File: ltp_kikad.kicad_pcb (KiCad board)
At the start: 2 copper layers, 65 x 56.5 mm, 21 parts, among them IC1 SamacSys_Parts_HT16K33-28SOP, IC2 SamacSys_Parts_HT16K33-28SOP, J2 RPi_GPIO

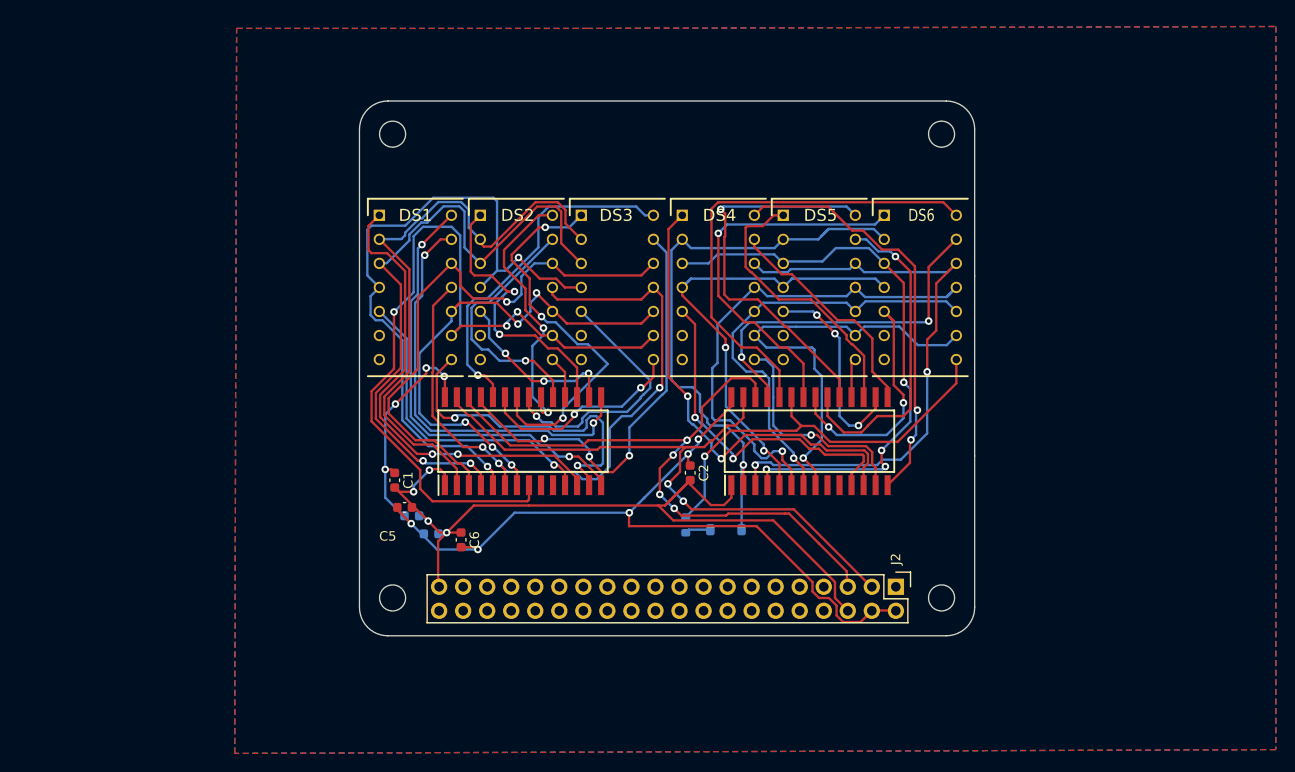
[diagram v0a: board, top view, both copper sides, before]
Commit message: Add 3d  device render
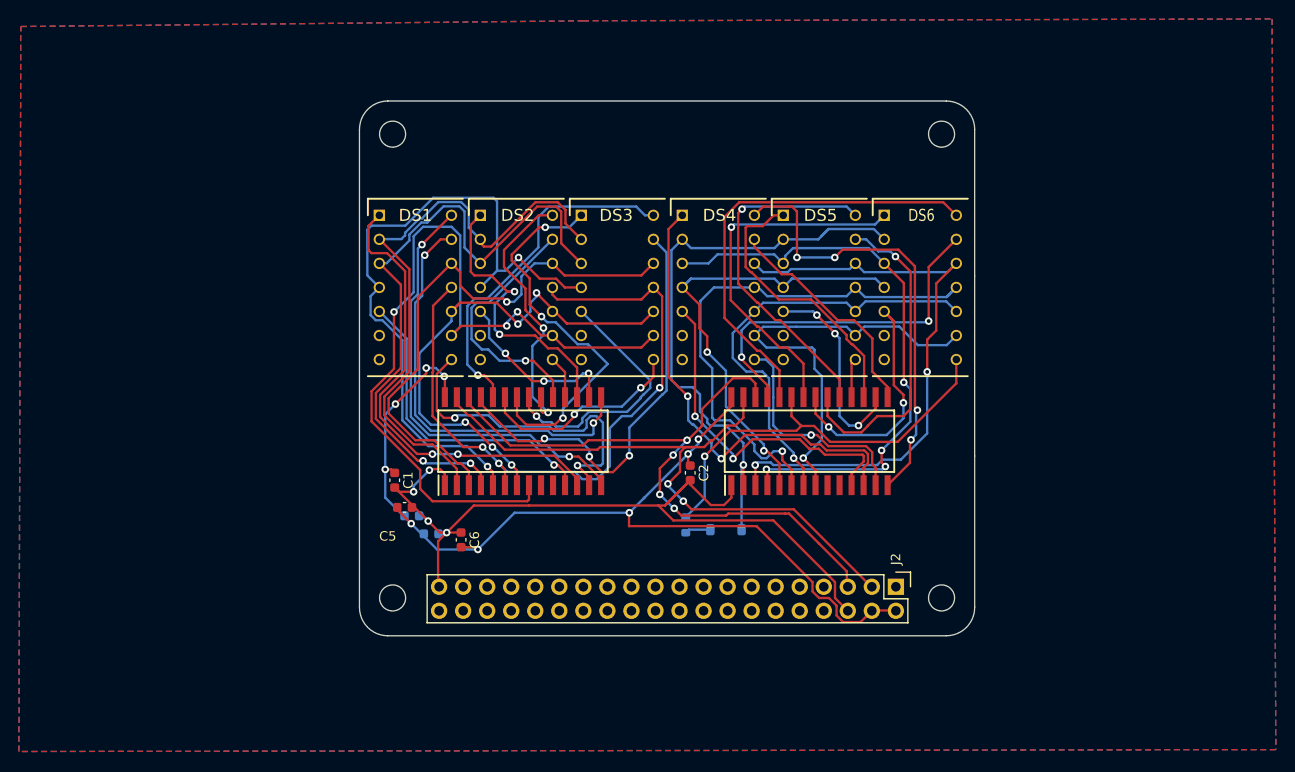
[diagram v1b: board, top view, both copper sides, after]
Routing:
- net 2_an6: track 42.2 -> 37.3 mm
- net 2_ca4: track 53.5 -> 57.0 mm
- net 2_an11: track 44.5 -> 48.0 mm, vias 2 -> 4
- net 2_an1: track 50.6 -> 47.3 mm
- net 2_an3: track 40.4 -> 38.4 mm

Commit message: Minimize vias transitions, optimize traces
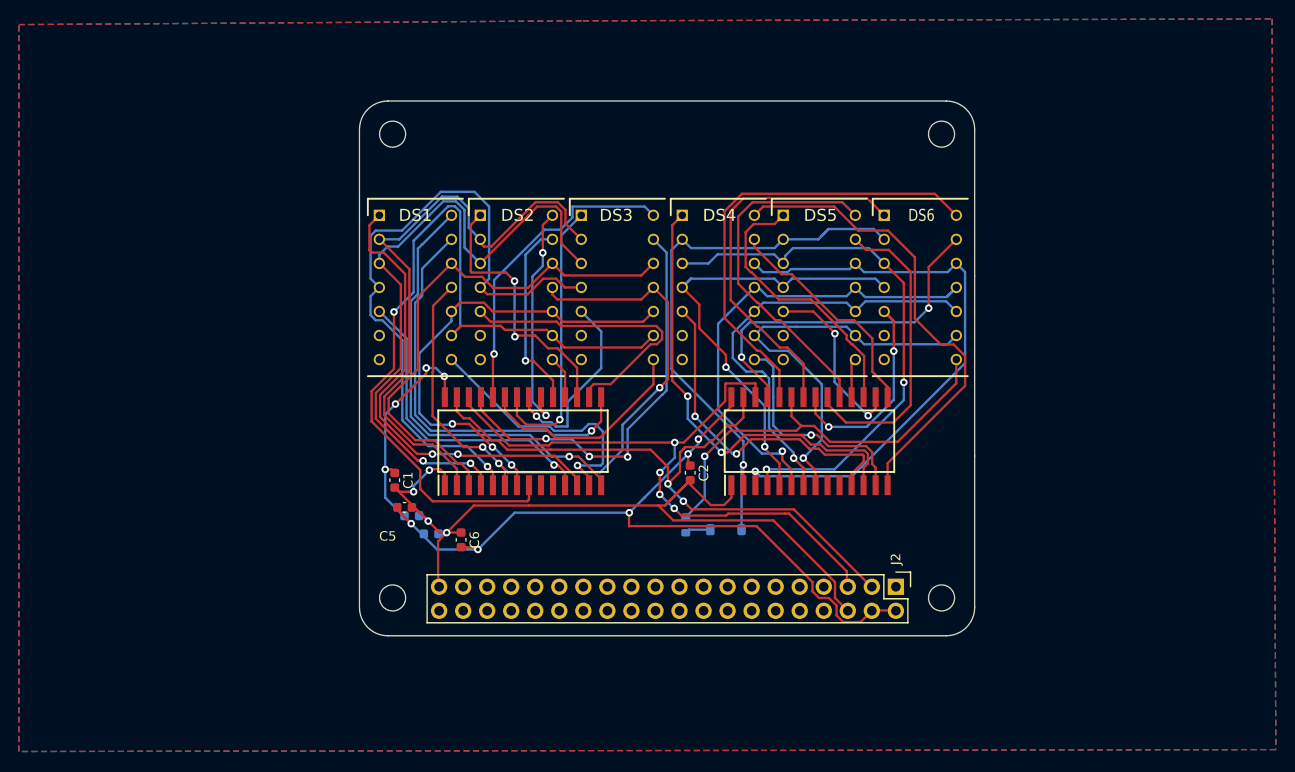
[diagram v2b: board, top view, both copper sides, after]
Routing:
- net an9: track 18.5 -> 31.7 mm, vias 3 -> 0
- net an3: track 41.2 -> 29.6 mm, vias 3 -> 1
- net an12: track 35.8 -> 28.5 mm, vias 2 -> 1
- net an4: track 27.9 -> 20.6 mm
- net an6: track 27.0 -> 20.2 mm
- net 2_ca4: track 57.0 -> 51.3 mm
- net an5: track 29.0 -> 24.8 mm
- net ca5: track 54.9 -> 50.9 mm, vias 5 -> 3
- net an1: track 37.4 -> 33.5 mm
- net 2_ca2: track 62.0 -> 58.1 mm, vias 4 -> 2
- net 2_an4: track 26.1 -> 22.8 mm
- net ca1: track 58.8 -> 55.6 mm, vias 1 -> 0
- net 2_an9: track 21.5 -> 18.9 mm, vias 3 -> 2
- net 2_an3: track 38.4 -> 41.0 mm, vias 1 -> 0
- net 2_ca6: track 46.7 -> 44.1 mm
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
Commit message: Minor improvements
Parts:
- moved J2 0.09 mm to (151.5, 105.6)
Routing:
- net SDA: track 68.5 -> 67.4 mm
- net +5V: track 108.7 -> 109.5 mm

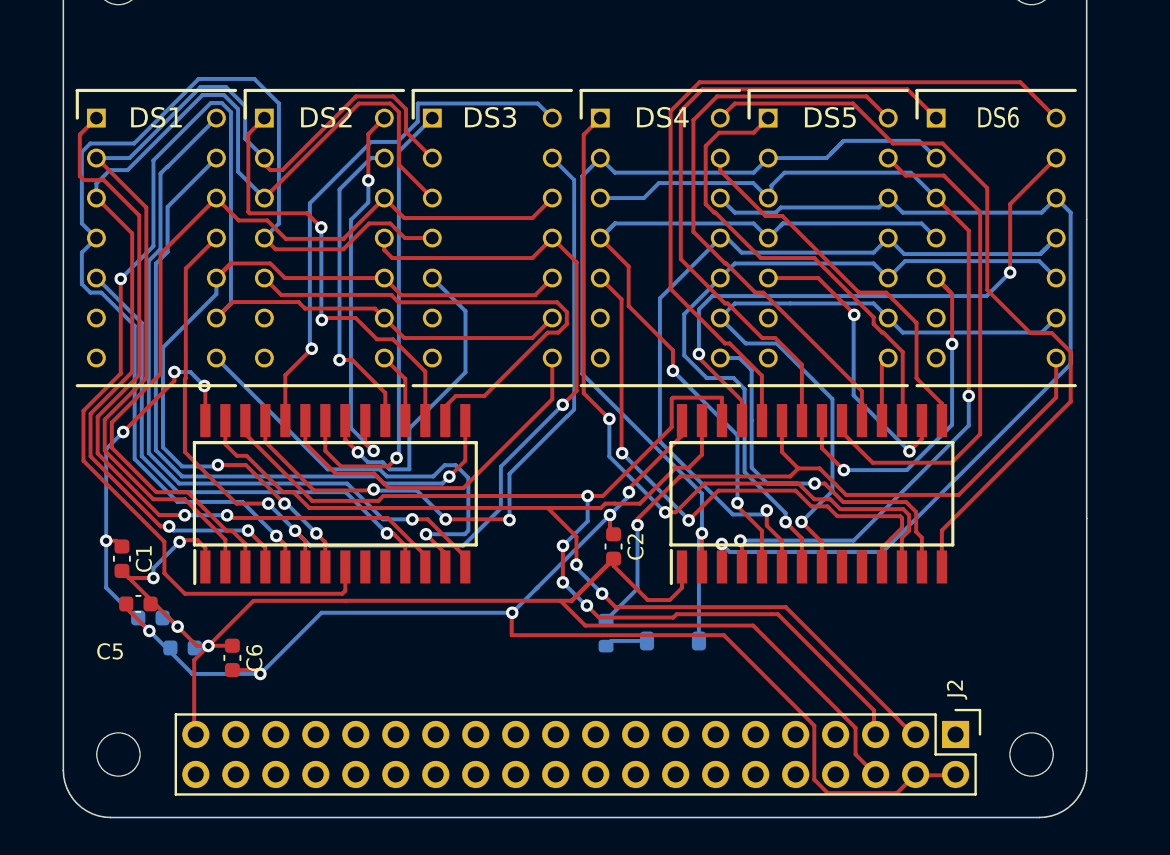
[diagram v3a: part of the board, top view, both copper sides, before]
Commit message: Add bypas cap
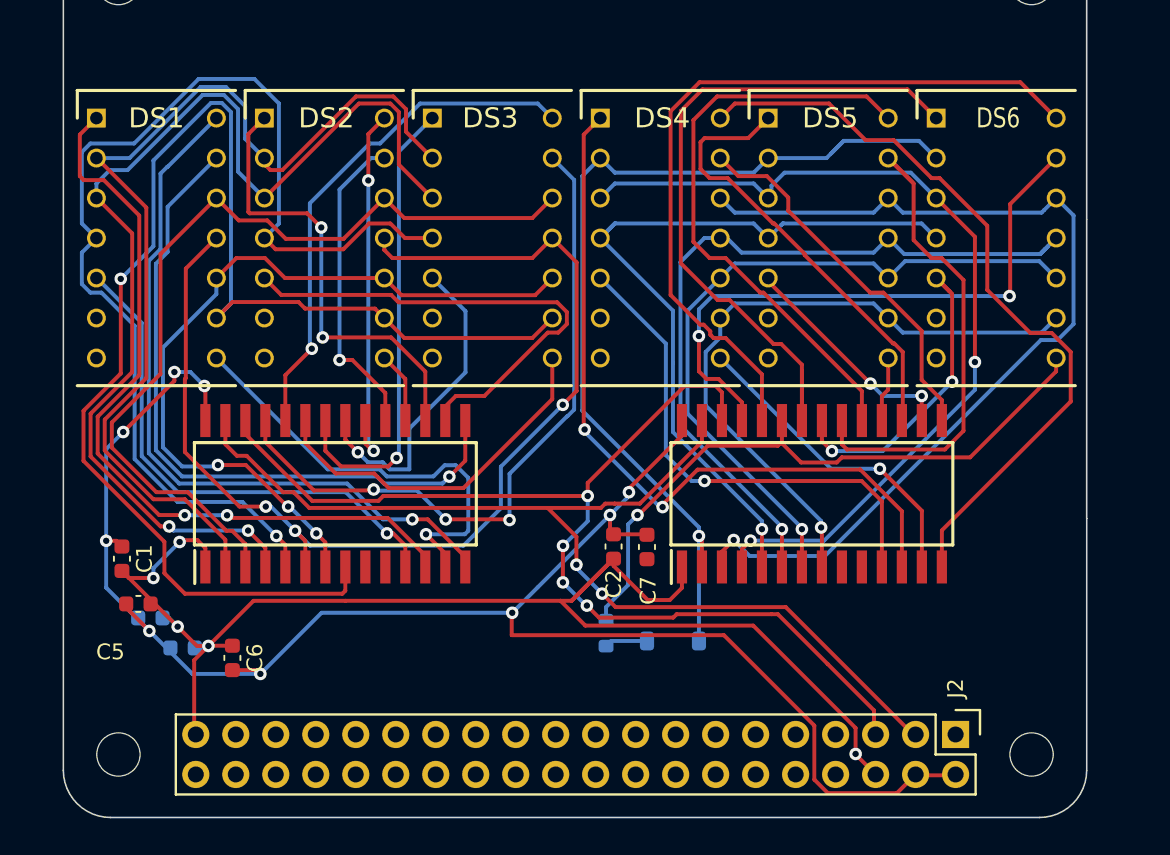
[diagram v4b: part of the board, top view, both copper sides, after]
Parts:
- added C7: 10uF, Capacitor_SMD:C_0603_1608Metric, F.Cu at (156.0, 92.4)
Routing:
- net 2_an9: track 18.9 -> 14.5 mm
- net 2_an14: track 36.4 -> 32.1 mm, vias 2 -> 1
- net 2_an12: track 23.8 -> 20.4 mm
- net 2_an2: track 44.4 -> 41.2 mm
- net 2_an4: track 22.8 -> 20.0 mm
- net 2_an3: track 41.0 -> 43.2 mm
- net 2_ca4: track 51.3 -> 49.2 mm
- net 2_ca6: track 44.1 -> 42.1 mm
- net +5V: track 109.5 -> 111.4 mm
- net 2_an11: track 50.0 -> 48.6 mm
- net 2_an0: track 37.4 -> 38.7 mm
- net 2_ca2: track 58.1 -> 56.8 mm
- net 2_ca5: track 46.4 -> 45.2 mm
- net 2_ca1: track 62.6 -> 61.5 mm
- net ca5: track 50.9 -> 49.9 mm
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
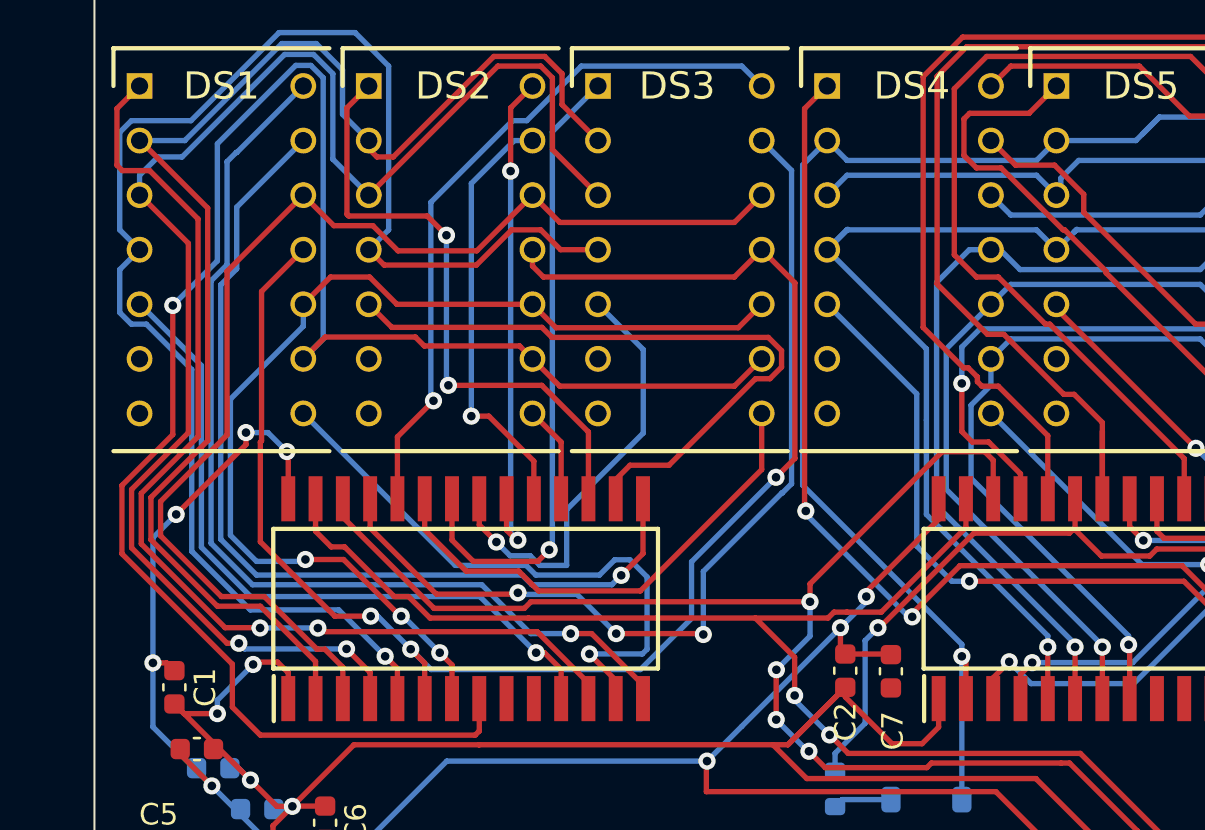
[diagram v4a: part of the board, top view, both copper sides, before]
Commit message: Optimize connection routes
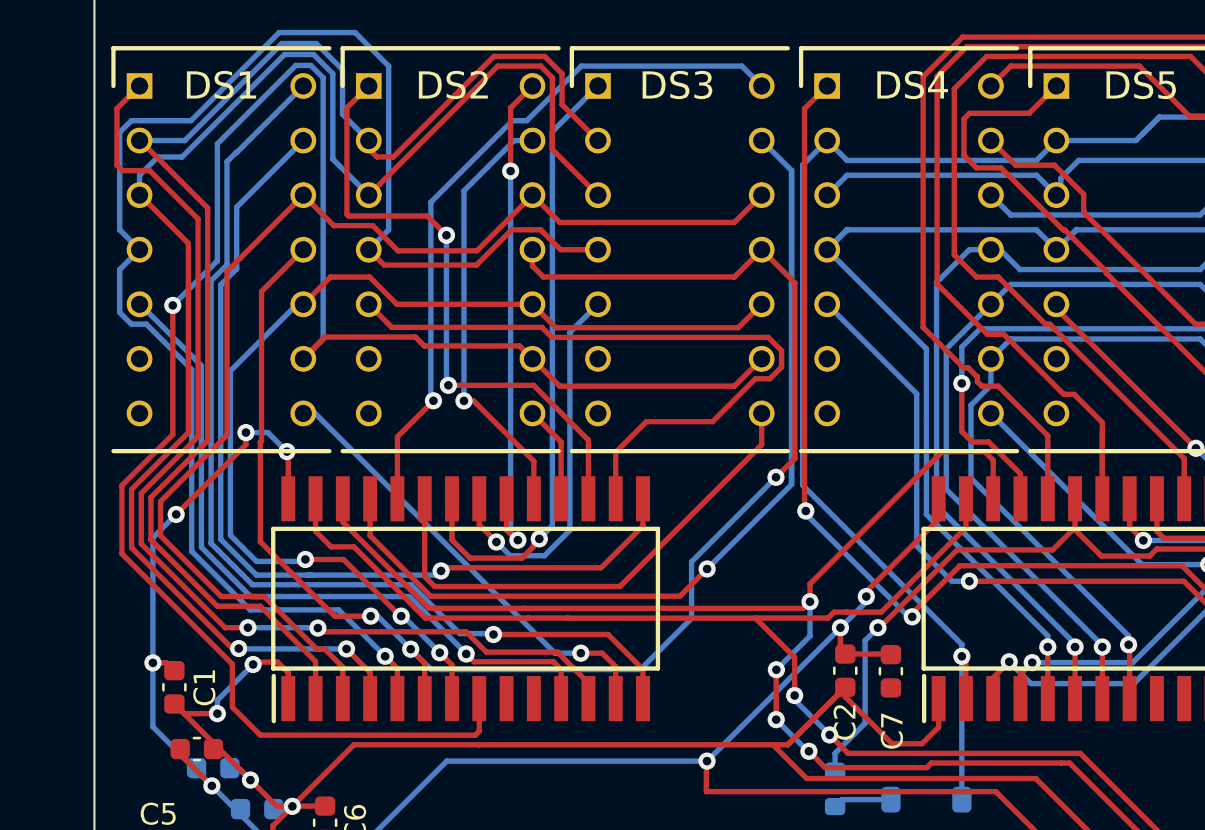
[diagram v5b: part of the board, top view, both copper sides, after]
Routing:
- net an0: track 44.3 -> 55.8 mm, vias 3 -> 1
- net an12: track 28.5 -> 20.9 mm
- net an4: track 20.6 -> 17.6 mm
- net an10: track 43.8 -> 42.9 mm
- net an9: track 31.7 -> 32.4 mm
- net an3: track 29.6 -> 29.0 mm

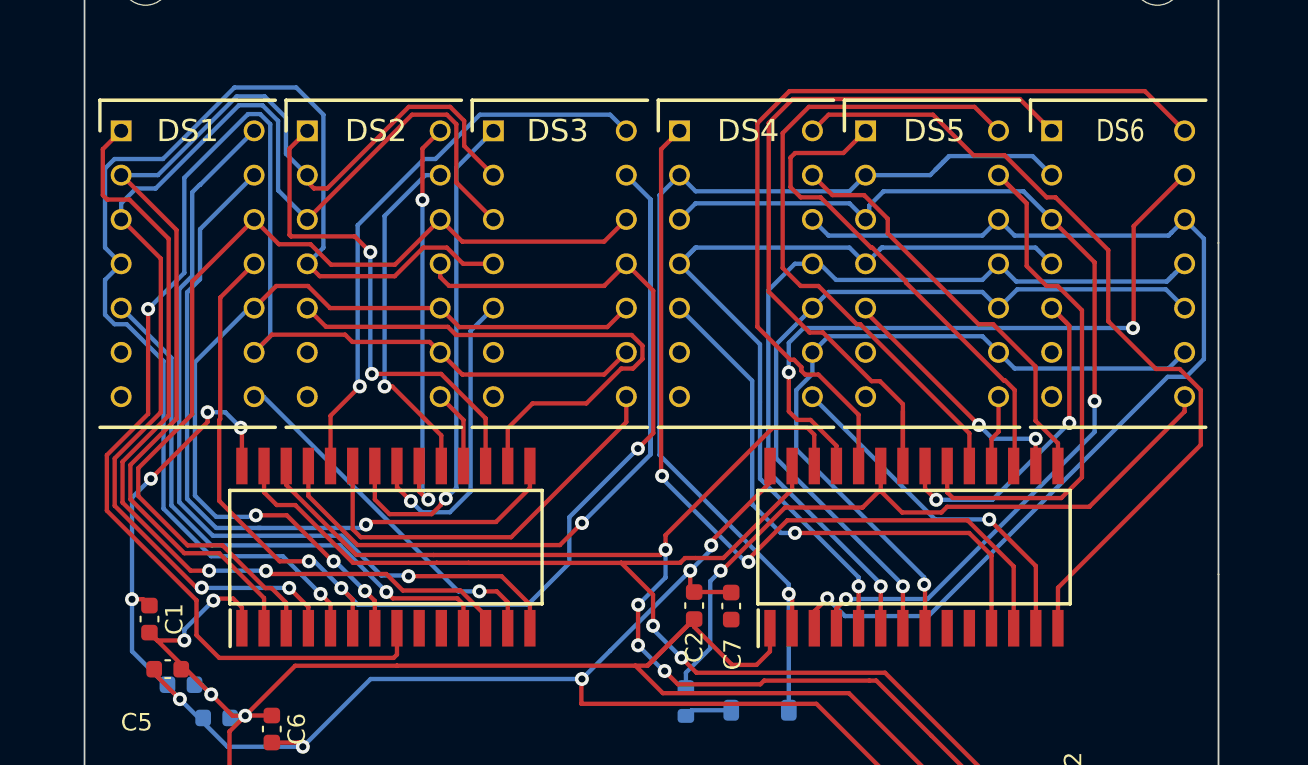
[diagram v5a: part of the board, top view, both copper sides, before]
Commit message: Shorten some routes
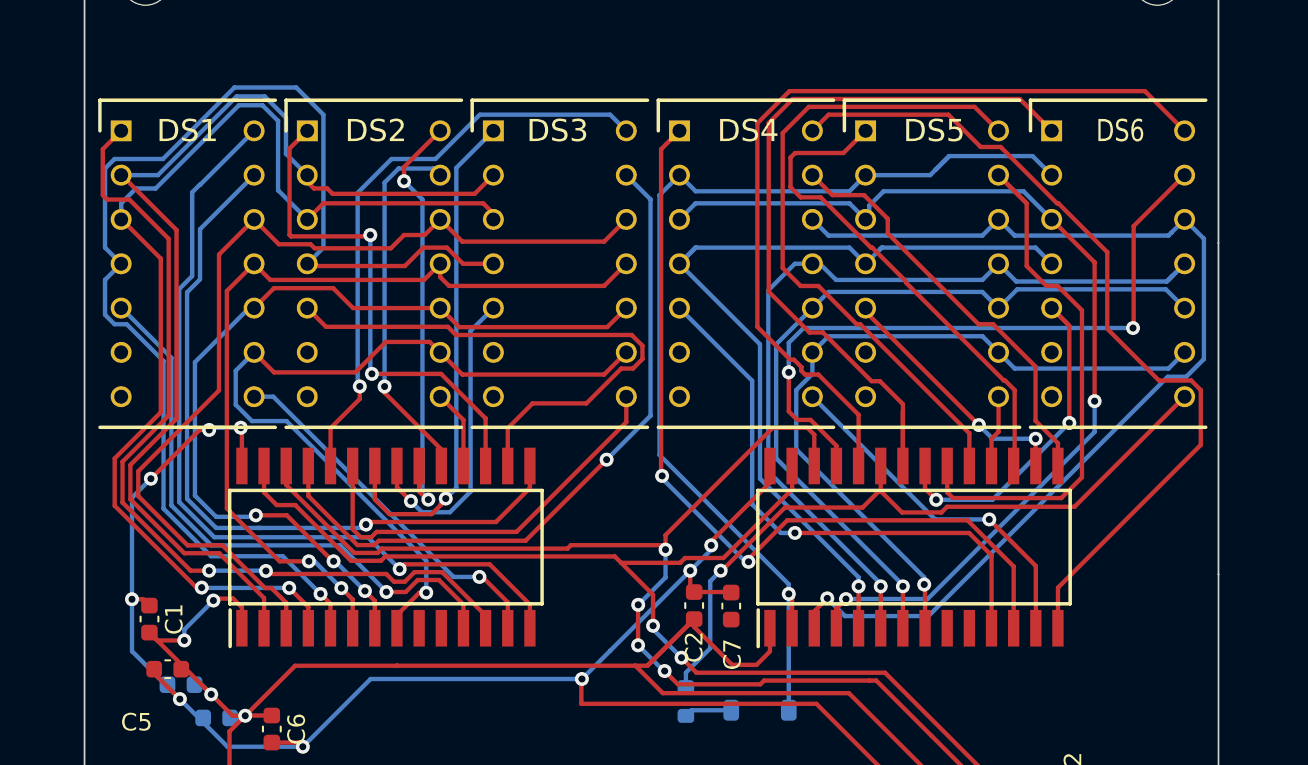
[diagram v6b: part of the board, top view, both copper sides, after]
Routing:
- net ca6: track 87.2 -> 46.7 mm
- net ca4: track 72.5 -> 49.3 mm, vias 3 -> 2
- net an0: track 55.8 -> 39.9 mm
- net ca2: track 69.9 -> 63.9 mm
- net ca0: track 63.6 -> 59.8 mm
- net an6: track 20.1 -> 21.3 mm
- net an1: track 33.0 -> 34.0 mm
- net +5V: track 111.4 -> 110.4 mm
- net an5: track 23.9 -> 24.8 mm
- net ca1: track 55.6 -> 54.8 mm
- net an8: track 28.8 -> 29.4 mm
- net an14: track 33.0 -> 33.6 mm

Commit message: Minor fixes
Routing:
- net ca3: track 70.9 -> 64.3 mm
- net 2_an2: track 40.7 -> 43.2 mm
- net 2_an13: track 48.2 -> 46.5 mm
- net 2_an12: track 20.4 -> 22.0 mm
- net 2_an14: track 32.1 -> 30.8 mm

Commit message: Minor improvements
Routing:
- net ca4: track 49.3 -> 57.2 mm, vias 2 -> 1
- net an8: track 29.4 -> 26.2 mm, vias 2 -> 1
- net +5V: track 110.4 -> 109.8 mm, vias 9 -> 7
